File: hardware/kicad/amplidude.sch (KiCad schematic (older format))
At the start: 29 parts

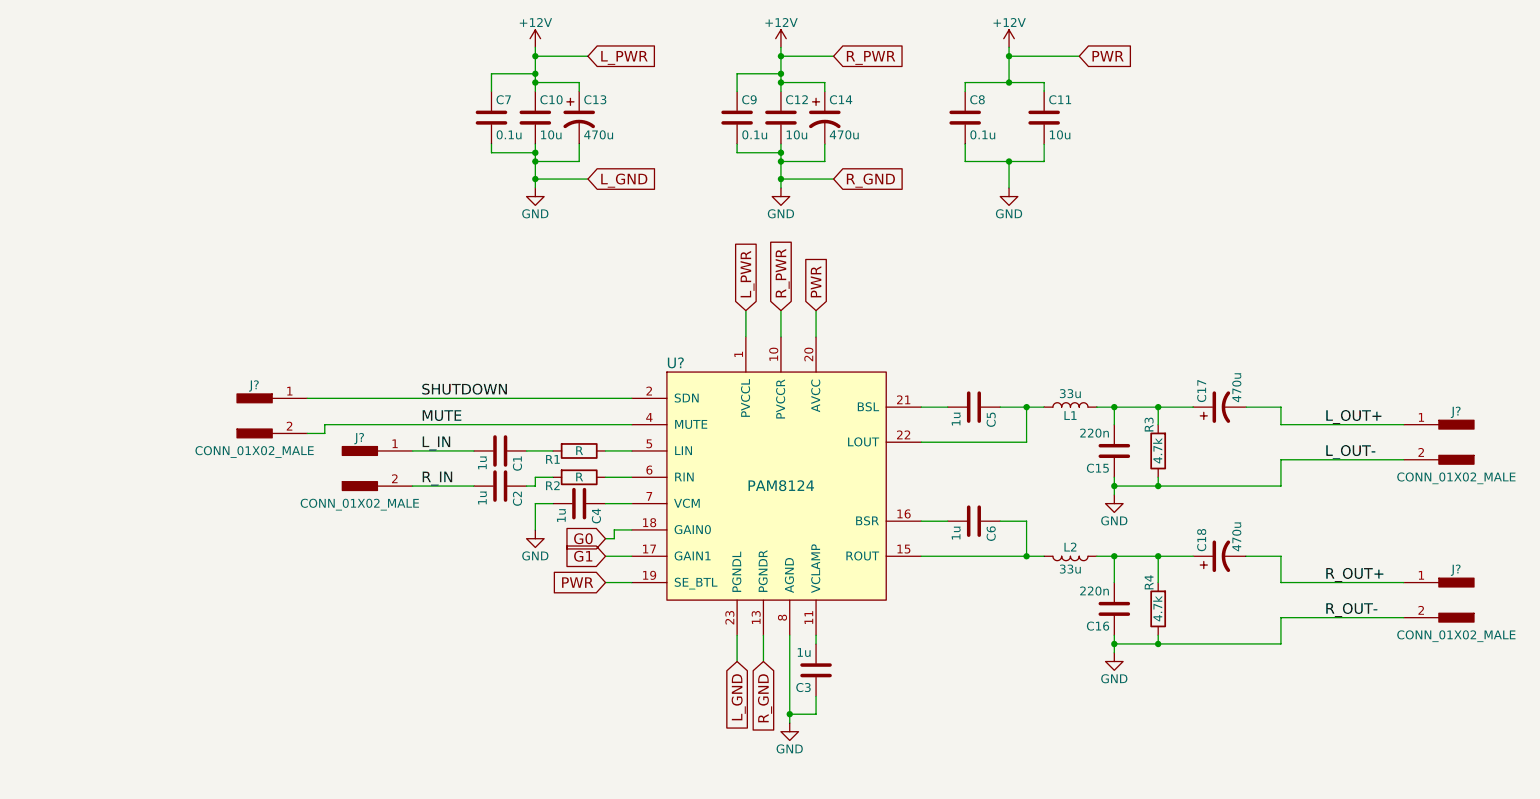
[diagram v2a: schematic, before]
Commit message: Connect MUTE and SHUTDOWN to jumper pins
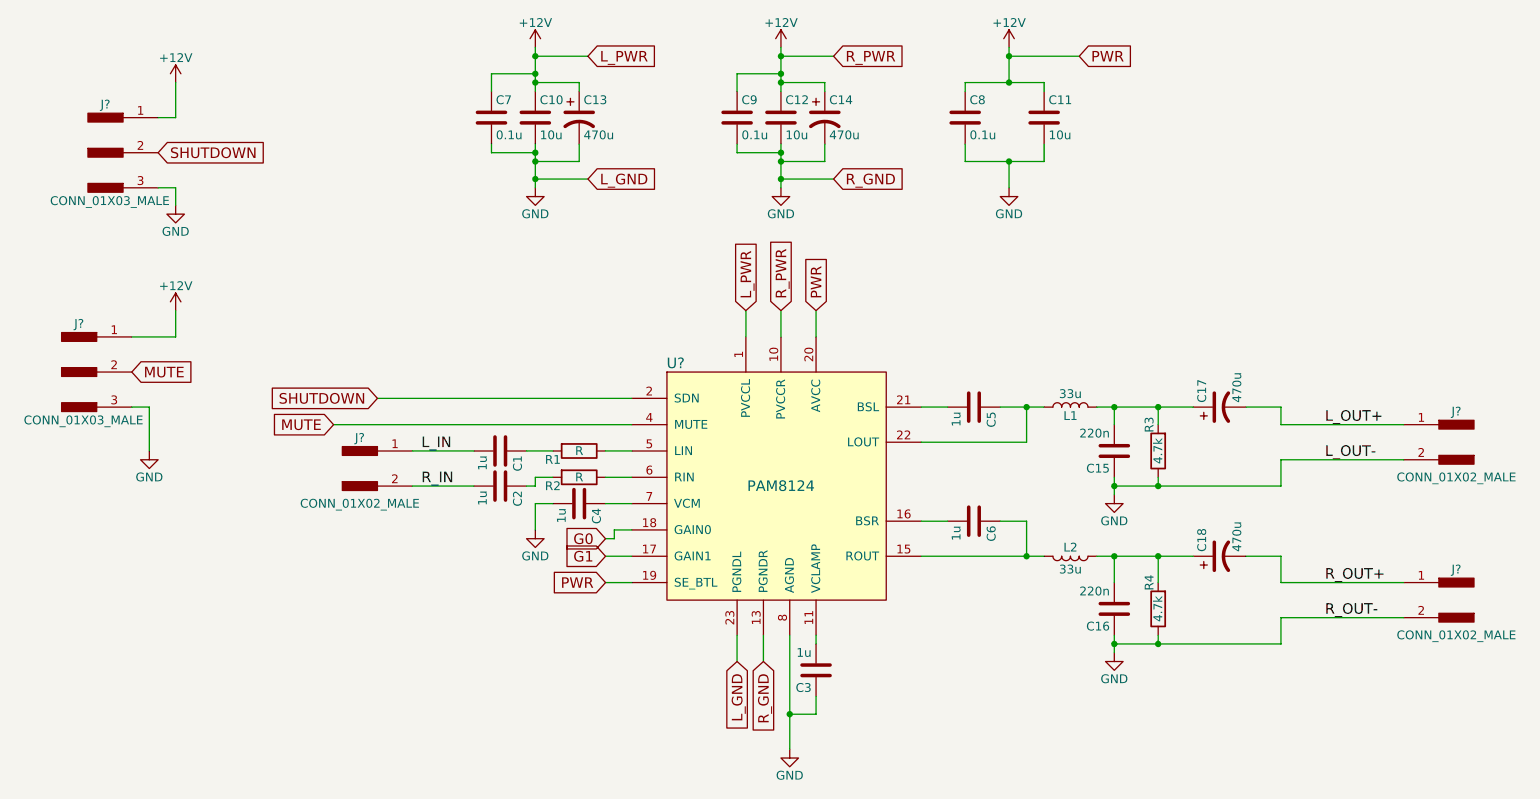
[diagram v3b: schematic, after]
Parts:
- removed J?: CONN_01X02_MALE, symbol CONN_01X02_MALE
- added J? (x2): CONN_01X03_MALE, symbol CONN_01X03_MALE
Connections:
- net +12V: now also J?.1, J?.1
- net AGND: now also J?.3, J?.3
- net MUTE: now also J?.2
- net SHUTDOWN: now also J?.2
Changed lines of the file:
@@
 L GND #PWR?
 U 1 1 5965A943
-P 5400 5450
-F 0 "#PWR?" H 5400 5200 50  0001 C CNN
-F 1 "GND" H 5400 5300 50  0000 C CNN
-F 2 "" H 5400 5450 50  0001 C CNN
-F 3 "" H 5400 5450 50  0001 C CNN
-	1    5400 5450
-	1    0    0    -1
-$EndComp
-Wire Wire Line
-	5400 4950 5400 5450
+P 5400 5600
+F 0 "#PWR?" H 5400 5350 50  0001 C CNN
+F 1 "GND" H 5400 5450 50  0000 C CNN
+F 2 "" H 5400 5600 50  0001 C CNN
+F 3 "" H 5400 5600 50  0001 C CNN
+	1    5400 5600
+	1    0    0    -1
+$EndComp
+Wire Wire Line
+	5400 4950 5400 5400
+Wire Wire Line
+	5400 5400 5400 5600
 $Comp
 L GND #PWR?
@@
 	3950 4100 3900 4100
 Wire Wire Line
-	2750 3750 4500 3750
+	2800 3750 4500 3750
 $Comp
 L C C3
@@
 	6150 4300 6300 4300
 Wire Wire Line
-	6150 4500 6850 4500
+	6150 4500 6750 4500
+Wire Wire Line
+	6750 4500 6850 4500
 Wire Wire Line
 	6150 3650 6300 3650
@@
 Connection ~ 6750 4500
 Wire Wire Line
-	6600 3650 6850 3650
+	6600 3650 6750 3650
+Wire Wire Line
+	6750 3650 6850 3650
 $Comp
 L C C15
@@
 $EndComp
 Wire Wire Line
-	7150 4500 7700 4500
+	7150 4500 7250 4500
+Wire Wire Line
+	7250 4500 7500 4500
+Wire Wire Line
+	7500 4500 7700 4500
 Wire Wire Line
 	7250 4500 7250 4650
 Wire Wire Line
-	7150 3650 7700 3650
+	7150 3650 7250 3650
+Wire Wire Line
+	7250 3650 7500 3650
+Wire Wire Line
+	7500 3650 7700 3650
 Wire Wire Line
 	7250 3650 7250 3750
@@
 $EndComp
 Wire Wire Line
-	7250 4950 7250 5050
-Wire Wire Line
-	7250 4050 7250 4150
+	7250 4950 7250 5000
+Wire Wire Line
+	7250 5000 7250 5050
+Wire Wire Line
+	7250 4050 7250 4100
+Wire Wire Line
+	7250 4100 7250 4150
 $Comp
 L R R3
@@
 	7500 4050 7500 4100
 Wire Wire Line
-	7250 4100 8200 4100
+	7250 4100 7500 4100
+Wire Wire Line
+	7500 4100 8200 4100
 $Comp
 L CP1 C17
@@
 Connection ~ 7250 4100
 Wire Wire Line
-	7250 5000 8200 5000
+	7250 5000 7500 5000
+Wire Wire Line
+	7500 5000 8200 5000
 Connection ~ 7250 5000
 Text GLabel 4350 4400 0    60   Input ~ 0
@@
 	5100 5100 5100 4950
 Wire Wire Line
-	2650 3600 4500 3600
+	3050 3600 4500 3600
 $Comp
 L +12V #PWR?
@@
 $EndComp
 Wire Wire Line
-	3950 2150 3950 2400
+	3950 2150 3950 2200
+Wire Wire Line
+	3950 2200 3950 2250
+Wire Wire Line
+	3950 2250 3950 2350
+Wire Wire Line
+	3950 2350 3950 2400
 Wire Wire Line
 	4200 2150 4200 2250
@@
 Connection ~ 3950 2200
 Wire Wire Line
-	3950 1600 3950 1850
+	3950 1600 3950 1650
+Wire Wire Line
+	3950 1650 3950 1750
+Wire Wire Line
+	3950 1750 3950 1800
+Wire Wire Line
+	3950 1800 3950 1850
 Wire Wire Line
 	3700 1850 3700 1750
@@
 $EndComp
 Wire Wire Line
-	5350 2150 5350 2400
+	5350 2150 5350 2200
+Wire Wire Line
+	5350 2200 5350 2250
+Wire Wire Line
+	5350 2250 5350 2350
+Wire Wire Line
+	5350 2350 5350 2400
 Wire Wire Line
 	5600 2150 5600 2250
@@
 Connection ~ 5350 2200
 Wire Wire Line
-	5350 1600 5350 1850
+	5350 1600 5350 1650
+Wire Wire Line
+	5350 1650 5350 1750
+Wire Wire Line
+	5350 1750 5350 1800
+Wire Wire Line
+	5350 1800 5350 1850
 Wire Wire Line
 	5100 1850 5100 1750
@@
 $EndComp
 Wire Wire Line
-	6650 1600 6650 1800
-Wire Wire Line
-	6400 1800 6850 1800
+	6650 1600 6650 1650
+Wire Wire Line
+	6650 1650 6650 1800
+Wire Wire Line
+	6400 1800 6650 1800
+Wire Wire Line
+	6650 1800 6850 1800
 Wire Wire Line
 	6400 1800 6400 1850
@@
 	6400 2150 6400 2250
 Wire Wire Line
-	6400 2250 6850 2250
+	6400 2250 6650 2250
+Wire Wire Line
+	6650 2250 6850 2250
 Wire Wire Line
 	6650 2250 6650 2400
@@
 Text Label 3300 4100 0    60   ~ 0
 R_IN
-$Comp
-L CONN_01X02_MALE J?
-U 1 1 596BE036
-P 2350 3700
-F 0 "J?" H 2350 3875 50  0000 C CNN
-F 1 "CONN_01X02_MALE" H 2350 3500 50  0000 C CNN
-F 2 "" H 2350 3800 50  0001 C CNN
-F 3 "" H 2350 3800 50  0001 C CNN
-	1    2350 3700
-	1    0    0    -1
-$EndComp
-Wire Wire Line
-	2750 3750 2750 3800
-Wire Wire Line
-	2750 3800 2650 3800
-Text Label 3300 3600 0    60   ~ 0
-SHUTDOWN
-Text Label 3300 3750 0    60   ~ 0
-MUTE
 $Comp
 L CONN_01X02_MALE J?
@@
 Text Label 8450 4850 0    60   ~ 0
 R_OUT-
+$Comp
+L CONN_01X03_MALE J?
+U 1 1 596C3CD1
+P 1500 2200
+F 0 "J?" H 1500 2475 50  0000 C CNN
+F 1 "CONN_01X03_MALE" H 1525 1925 50  0000 C CNN
+F 2 "" H 1500 2400 50  0001 C CNN
+F 3 "" H 1500 2400 50  0001 C CNN
+	1    1500 2200
+	1    0    0    -1
+$EndComp
+$Comp
+L CONN_01X03_MALE J?
+U 1 1 596C3D4D
+P 1350 3450
+F 0 "J?" H 1350 3725 50  0000 C CNN
+F 1 "CONN_01X03_MALE" H 1375 3175 50  0000 C CNN
+F 2 "" H 1350 3650 50  0001 C CNN
+F 3 "" H 1350 3650 50  0001 C CNN
+	1    1350 3450
+	1    0    0    -1
+$EndComp
+$Comp
+L +12V #PWR?
+U 1 1 596C403C
+P 1900 1800
+F 0 "#PWR?" H 1900 1650 50  0001 C CNN
+F 1 "+12V" H 1900 1940 50  0000 C CNN
+F 2 "" H 1900 1800 50  0001 C CNN
+F 3 "" H 1900 1800 50  0001 C CNN
+	1    1900 1800
+	1    0    0    -1
+$EndComp
+$Comp
+L +12V #PWR?
+U 1 1 596C40A1
+P 1900 3100
+F 0 "#PWR?" H 1900 2950 50  0001 C CNN
+F 1 "+12V" H 1900 3240 50  0000 C CNN
+F 2 "" H 1900 3100 50  0001 C CNN
+F 3 "" H 1900 3100 50  0001 C CNN
+	1    1900 3100
+	1    0    0    -1
+$EndComp
+Wire Wire Line
+	1650 3250 1900 3250
+Wire Wire Line
+	1900 3250 1900 3100
+Wire Wire Line
+	1800 2000 1900 2000
+Wire Wire Line
+	1900 2000 1900 1800
+$Comp
+L GND #PWR?
+U 1 1 596C429C
+P 1750 3900
+F 0 "#PWR?" H 1750 3650 50  0001 C CNN
+F 1 "GND" H 1750 3750 50  0000 C CNN
+F 2 "" H 1750 3900 50  0001 C CNN
+F 3 "" H 1750 3900 50  0001 C CNN
+	1    1750 3900
+	1    0    0    -1
+$EndComp
+Wire Wire Line
+	1650 3650 1750 3650
+Wire Wire Line
+	1750 3650 1750 3900
+$Comp
+L GND #PWR?
+U 1 1 596C439D
+P 1900 2500
+F 0 "#PWR?" H 1900 2250 50  0001 C CNN
+F 1 "GND" H 1900 2350 50  0000 C CNN
+F 2 "" H 1900 2500 50  0001 C CNN
+F 3 "" H 1900 2500 50  0001 C CNN
+	1    1900 2500
+	1    0    0    -1
+$EndComp
+Wire Wire Line
+	1800 2400 1900 2400
+Wire Wire Line
+	1900 2400 1900 2500
+Text GLabel 3050 3600 0    60   Input ~ 0
+SHUTDOWN
+Text GLabel 2800 3750 0    60   Input ~ 0
+MUTE
+Text GLabel 1800 2200 2    60   Input ~ 0
+SHUTDOWN
+Text GLabel 1650 3450 2    60   Input ~ 0
+MUTE
 $EndSCHEMATC
